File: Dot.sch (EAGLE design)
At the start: 43 parts, among them IC1 CAT24M010TS, IC2 SI1145, U1 ATMEGA328P-MU-QFN32, U2 TMP102, U3 ISL29125, U4 9DoF IMU, U5 BMP18

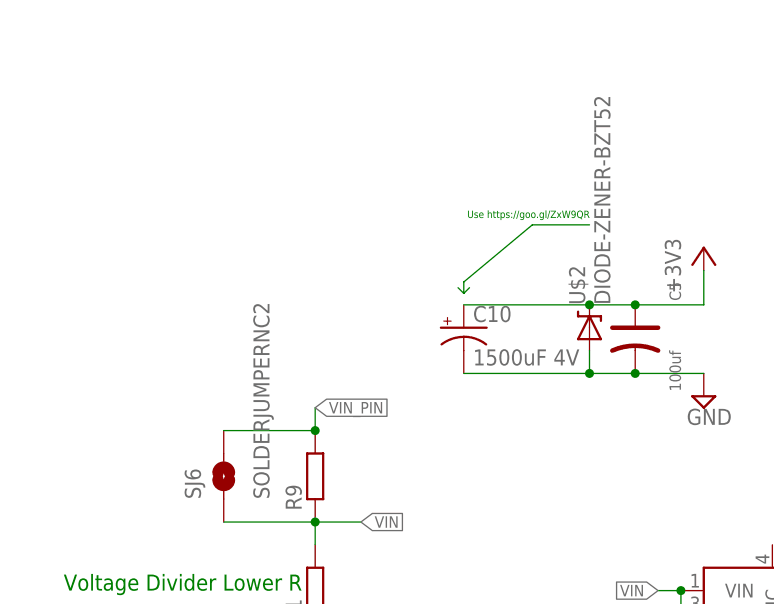
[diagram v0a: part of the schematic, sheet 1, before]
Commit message: Update description : Use a Schottky instead of R9 for solar cell
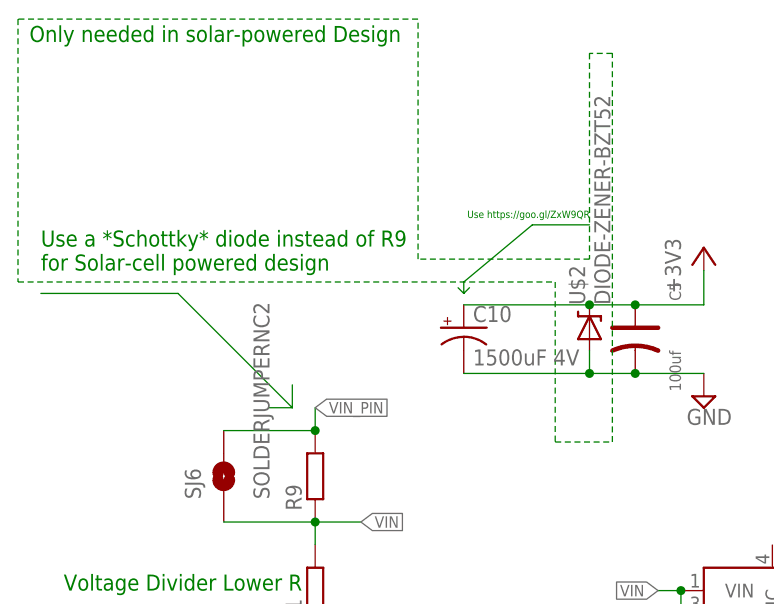
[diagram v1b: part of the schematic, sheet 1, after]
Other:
- note added: "Only needed in solar-powered Design"
- note added: "Use a *Schottky* diode instead of R9 for Solar-cell powered design"
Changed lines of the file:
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@@
 <setting verticaltext="up"/>
 </settings>
-<grid distance="1.27" unitdist="mm" unit="mm" style="lines" multiple="1" display="no" altdistance="0.01" altunitdist="inch" altunit="inch"/>
+<grid distance="0.1" unitdist="inch" unit="inch" style="lines" multiple="1" display="no" altdistance="0.01" altunitdist="inch" altunit="inch"/>
 <layers>
 <layer number="1" name="Top" color="4" fill="1" visible="no" active="no"/>
@@
 <text x="-60.96" y="134.62" size="1.778" layer="91">Voltage Divider Lower R</text>
 <text x="-16.129" y="176.022" size="0.8128" layer="91">Use https://goo.gl/ZxW9QR</text>
+<text x="-63.5" y="170.18" size="1.778" layer="91">Use a *Schottky* diode instead of R9
+for Solar-cell powered design</text>
+<text x="-64.77" y="195.58" size="1.778" layer="91">Only needed in solar-powered Design</text>
 </plain>
 <instances>
@@
 </segment>
 </net>
+<net name="N$9" class="0">
+<segment>
+<wire x1="-63.5" y1="167.64" x2="-48.26" y2="167.64" width="0.1524" layer="91"/>
+<wire x1="-48.26" y1="167.64" x2="-35.56" y2="154.94" width="0.1524" layer="91"/>
+<wire x1="-35.56" y1="154.94" x2="-35.56" y2="157.48" width="0.1524" layer="91"/>
+<wire x1="-35.56" y1="154.94" x2="-38.1" y2="154.94" width="0.1524" layer="91"/>
+</segment>
+</net>
+<net name="N$12" class="0">
+<segment>
+<wire x1="-66.04" y1="168.91" x2="-6.35" y2="168.91" width="0.1524" layer="91" style="shortdash"/>
+<wire x1="-6.35" y1="168.91" x2="-6.35" y2="151.13" width="0.1524" layer="91" style="shortdash"/>
+<wire x1="-6.35" y1="151.13" x2="0" y2="151.13" width="0.1524" layer="91" style="shortdash"/>
+<wire x1="0" y1="151.13" x2="0" y2="194.31" width="0.1524" layer="91" style="shortdash"/>
+<wire x1="0" y1="194.31" x2="-2.54" y2="194.31" width="0.1524" layer="91" style="shortdash"/>
+<wire x1="-2.54" y1="194.31" x2="-2.54" y2="171.45" width="0.1524" layer="91" style="shortdash"/>
+<wire x1="-2.54" y1="171.45" x2="-21.59" y2="171.45" width="0.1524" layer="91" style="shortdash"/>
+<wire x1="-21.59" y1="171.45" x2="-21.59" y2="198.12" width="0.1524" layer="91" style="shortdash"/>
+<wire x1="-21.59" y1="198.12" x2="-66.04" y2="198.12" width="0.1524" layer="91" style="shortdash"/>
+<wire x1="-66.04" y1="198.12" x2="-66.04" y2="168.91" width="0.1524" layer="91" style="shortdash"/>
+</segment>
+</net>

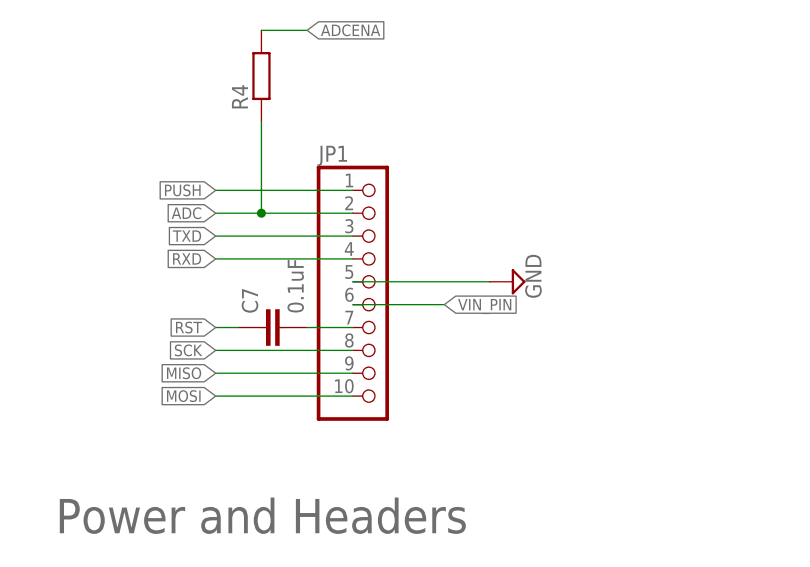
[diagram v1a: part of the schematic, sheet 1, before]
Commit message: Add jumper for C7 Reset
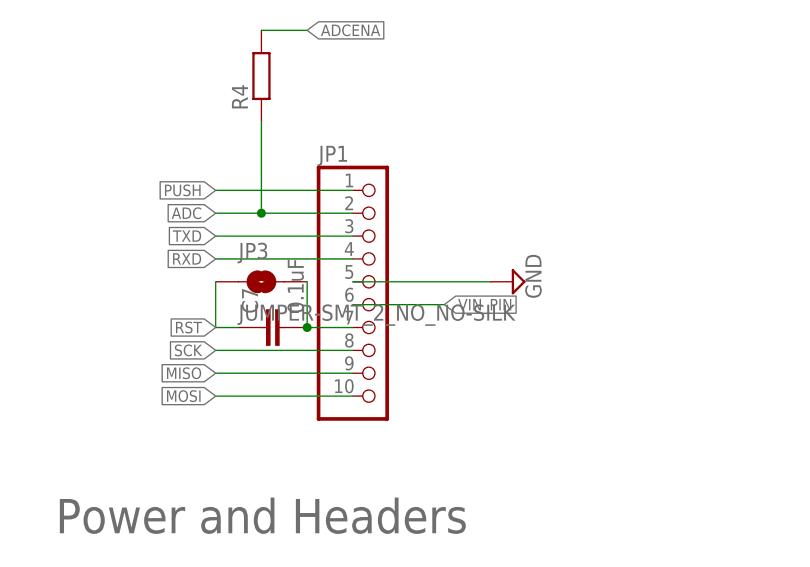
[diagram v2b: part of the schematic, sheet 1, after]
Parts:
- added JP3: JUMPER-SMT_2_NO_NO-SILK, SparkFun-Jumpers:JUMPER-SMT_2_NO_NO-SILK
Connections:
- net N$5: now also JP3.2
- net RST: now also JP3.1
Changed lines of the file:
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@@
 <part name="C10" library="adafruit" deviceset="CPOL-US" device="CT7343" value="1500uF 4V"/>
 <part name="U$2" library="SparkFun" deviceset="DIODE-ZENER" device="-BZT52"/>
+<part name="JP3" library="SparkFun-Jumpers" deviceset="JUMPER-SMT_2_NO" device="_NO-SILK"/>
 </parts>
 <sheets>
@@
 <instance part="C10" gate="G$1" x="-16.51" y="163.83"/>
 <instance part="U$2" gate="G$1" x="-2.54" y="163.83" rot="R90"/>
+<instance part="JP3" gate="G$1" x="66.04" y="134.62"/>
 </instances>
 <busses>
@@
 <wire x1="63.5" y1="129.54" x2="60.96" y2="129.54" width="0.1524" layer="91"/>
 <label x="60.96" y="129.54" size="1.27" layer="95" rot="R180" xref="yes"/>
+<wire x1="60.96" y1="134.62" x2="60.96" y2="129.54" width="0.1524" layer="91"/>
+<pinref part="JP3" gate="G$1" pin="1"/>
 </segment>
 </net>
@@
 <pinref part="C7" gate="G$1" pin="2"/>
 <wire x1="76.2" y1="129.54" x2="71.12" y2="129.54" width="0.1524" layer="91"/>
-</segment>
-</net>
+<wire x1="71.12" y1="134.62" x2="71.12" y2="129.54" width="0.1524" layer="91"/>
+<junction x="71.12" y="129.54"/>
+<pinref part="JP3" gate="G$1" pin="2"/>
+</segment>
+</net>

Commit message: Added AT25SF081, fixed labels
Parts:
- removed C6: 1uF, resistor:C-EUC0603
- removed SJ6: SOLDERJUMPERNC2, SparkFun:SOLDERJUMPERNC2
- added JP4: JUMPER-SMT_2_NO_NO-SILK, SparkFun-Jumpers:JUMPER-SMT_2_NO_NO-SILK
- C7: value 0.1uF -> 1uF
- U$3: value AT45DB641E -> AT25SF081; device AT45DB641E:AT45DB641E -> AT25SF081:AT25SF081
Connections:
- net +3V3: now also U$3.NHOLD, U$3.WP; no longer C6.1, U$3.NRST
- net GND: no longer C6.2, U$3.PAD
- net VIN: now also JP4.2; no longer SJ6.1
- net VIN_PIN: now also JP4.1; no longer SJ6.2
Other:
- note added: "Use AT25SF081-MAHF-T"
- note removed: "use AT45DB641E-MHN-Y for starndard page size (1056b/page) or AT45DB641E-MHN2B-T for binary page size (1024b/page)"
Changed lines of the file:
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@@
 <part name="SUPPLY20" library="supply2" deviceset="GND" device=""/>
 <part name="U3" library="SparkFun-Sensors" deviceset="ISL29125" device=""/>
-<part name="C6" library="resistor" deviceset="C-EU" device="C0603" value="1uF"/>
 <part name="SUPPLY21" library="supply2" deviceset="GND" device=""/>
 <part name="U4" library="SparkFun-Sensors" deviceset="MPU-9250" device="" value="9DoF IMU"/>
@@
 <part name="+3V14" library="supply1" deviceset="+3V3" device=""/>
 <part name="U5" library="Seeed-OPL-sensor" deviceset="PRESSURE-BMP180(LGA7)" device="" value="BMP18"/>
-<part name="U$3" library="AT45DB641E" deviceset="AT45DB641E" device=""/>
 <part name="+3V15" library="supply1" deviceset="+3V3" device=""/>
 <part name="SUPPLY7" library="supply2" deviceset="GND" device=""/>
@@
 <part name="R9" library="resistor" deviceset="R-EU_" device="R0603"/>
 <part name="SJ3" library="SparkFun" deviceset="SOLDERJUMPER" device="NC2"/>
-<part name="C7" library="resistor" deviceset="C-EU" device="C0603" value="0.1uF"/>
-<part name="SJ6" library="SparkFun" deviceset="SOLDERJUMPER" device="NC2"/>
+<part name="C7" library="resistor" deviceset="C-EU" device="C0603" value="1uF"/>
 <part name="Y1" library="SparkFun-Clocks" deviceset="RESONATOR" device="SMD-3.2X1.3"/>
 <part name="SUPPLY30" library="supply2" deviceset="GND" device=""/>
@@
 <part name="U$2" library="SparkFun" deviceset="DIODE-ZENER" device="-BZT52"/>
 <part name="JP3" library="SparkFun-Jumpers" deviceset="JUMPER-SMT_2_NO" device="_NO-SILK"/>
+<part name="JP4" library="SparkFun-Jumpers" deviceset="JUMPER-SMT_2_NO" device="_NO-SILK"/>
+<part name="U$3" library="AT25SF081" deviceset="AT25SF081" device=""/>
 </parts>
 <sheets>
@@
 Humidity</text>
 <text x="175.26" y="0" size="1.016" layer="91" align="center">TMP102 or TMP112 (high acc +/-0.5°)</text>
-<text x="43.18" y="88.9" size="1.778" layer="91">use AT45DB641E-MHN-Y for starndard page size (1056b/page)
-or AT45DB641E-MHN2B-T for binary page size (1024b/page)</text>
 <text x="-24.13" y="50.8" size="1.27" layer="91">Blue</text>
 <text x="-7.62" y="50.8" size="1.27" layer="91" rot="R90">Green</text>
@@
 for Solar-cell powered design</text>
 <text x="-64.77" y="195.58" size="1.778" layer="91">Only needed in solar-powered Design</text>
+<text x="73.66" y="86.36" size="1.778" layer="91">Use AT25SF081-MAHF-T</text>
 </plain>
 <instances>
@@
 <instance part="SUPPLY20" gate="GND" x="264.16" y="-38.1" rot="MR0"/>
 <instance part="U3" gate="G$1" x="358.14" y="-27.94"/>
-<instance part="C6" gate="G$1" x="337.82" y="-27.94"/>
 <instance part="SUPPLY21" gate="GND" x="337.82" y="-35.56" rot="MR0"/>
 <instance part="U4" gate="G$1" x="78.74" y="-27.94"/>
@@
 <instance part="+3V14" gate="G$1" x="-10.16" y="81.28"/>
 <instance part="U5" gate="G$1" x="170.18" y="-50.8"/>
-<instance part="U$3" gate="G$1" x="60.96" y="68.58"/>
-<instance part="+3V15" gate="G$1" x="96.52" y="83.82"/>
-<instance part="SUPPLY7" gate="GND" x="91.44" y="73.66" rot="R90"/>
-<instance part="+3V17" gate="G$1" x="48.26" y="78.74"/>
-<instance part="SUPPLY8" gate="GND" x="73.66" y="81.28" rot="R90"/>
+<instance part="+3V15" gate="G$1" x="111.76" y="83.82"/>
+<instance part="SUPPLY7" gate="GND" x="66.04" y="68.58" rot="R270"/>
+<instance part="+3V17" gate="G$1" x="55.88" y="71.12" rot="R90"/>
+<instance part="SUPPLY8" gate="GND" x="45.72" y="93.98" rot="R90"/>
 <instance part="+3V18" gate="G$1" x="154.94" y="-43.18"/>
 <instance part="SUPPLY22" gate="GND" x="166.37" y="-60.96" rot="MR0"/>
@@
 <instance part="SJ3" gate="1" x="17.78" y="114.3"/>
 <instance part="C7" gate="G$1" x="66.04" y="129.54" rot="R90"/>
-<instance part="SJ6" gate="1" x="-43.18" y="147.32" rot="R90"/>
 <instance part="Y1" gate="G$1" x="200.66" y="66.04" rot="R90"/>
 <instance part="SUPPLY30" gate="GND" x="208.28" y="63.5"/>
@@
 <instance part="U$2" gate="G$1" x="-2.54" y="163.83" rot="R90"/>
 <instance part="JP3" gate="G$1" x="66.04" y="134.62"/>
+<instance part="JP4" gate="G$1" x="-43.18" y="147.32" rot="MR270"/>
+<instance part="U$3" gate="G$1" x="71.12" y="68.58"/>
 </instances>
 <busses>
@@
 </segment>
 <segment>
-<pinref part="C6" gate="G$1" pin="2"/>
 <pinref part="U3" gate="G$1" pin="GND"/>
 <wire x1="337.82" y1="-33.02" x2="347.98" y2="-33.02" width="0.1524" layer="91"/>
 <wire x1="347.98" y1="-33.02" x2="347.98" y2="-30.48" width="0.1524" layer="91"/>
-<junction x="337.82" y="-33.02"/>
 <pinref part="SUPPLY21" gate="GND" pin="GND"/>
 </segment>
@@
 </segment>
 <segment>
+<pinref part="SUPPLY7" gate="GND" pin="GND"/>
+<wire x1="71.12" y1="68.58" x2="68.58" y2="68.58" width="0.1524" layer="91"/>
 <pinref part="U$3" gate="G$1" pin="GND"/>
-<pinref part="SUPPLY7" gate="GND" pin="GND"/>
-<wire x1="81.28" y1="73.66" x2="88.9" y2="73.66" width="0.1524" layer="91"/>
-</segment>
-<segment>
-<pinref part="U$3" gate="G$1" pin="PAD"/>
-<pinref part="SUPPLY8" gate="GND" pin="GND"/>
 </segment>
 <segment>
@@
 <pinref part="+3V9" gate="G$1" pin="+3V3"/>
 <pinref part="C1" gate="G$1" pin="1"/>
-<pinref part="C6" gate="G$1" pin="1"/>
 <pinref part="U3" gate="G$1" pin="VDD"/>
-<wire x1="337.82" y1="-25.4" x2="347.98" y2="-25.4" width="0.1524" layer="91"/>
-<wire x1="327.66" y1="-25.4" x2="337.82" y2="-25.4" width="0.1524" layer="91"/>
+<wire x1="327.66" y1="-25.4" x2="347.98" y2="-25.4" width="0.1524" layer="91"/>
 <junction x="327.66" y="-25.4"/>
-<junction x="337.82" y="-25.4"/>
 </segment>
 <segment>
@@
 </segment>
 <segment>
+<pinref part="+3V15" gate="G$1" pin="+3V3"/>
+<wire x1="101.6" y1="76.2" x2="111.76" y2="76.2" width="0.1524" layer="91"/>
+<wire x1="111.76" y1="76.2" x2="111.76" y2="81.28" width="0.1524" layer="91"/>
 <pinref part="U$3" gate="G$1" pin="VCC"/>
-<pinref part="+3V15" gate="G$1" pin="+3V3"/>
-<wire x1="81.28" y1="71.12" x2="96.52" y2="71.12" width="0.1524" layer="91"/>
-<wire x1="96.52" y1="71.12" x2="96.52" y2="81.28" width="0.1524" layer="91"/>
-</segment>
-<segment>
-<pinref part="U$3" gate="G$1" pin="NRST"/>
+<pinref part="U$3" gate="G$1" pin="NHOLD"/>
+<wire x1="101.6" y1="73.66" x2="111.76" y2="73.66" width="0.1524" layer="91"/>
+<wire x1="111.76" y1="73.66" x2="111.76" y2="76.2" width="0.1524" layer="91"/>
+<junction x="111.76" y="76.2"/>
+</segment>
+<segment>
 <pinref part="+3V17" gate="G$1" pin="+3V3"/>
-<wire x1="60.96" y1="71.12" x2="48.26" y2="71.12" width="0.1524" layer="91"/>
-<wire x1="48.26" y1="71.12" x2="48.26" y2="76.2" width="0.1524" layer="91"/>
+<wire x1="71.12" y1="71.12" x2="58.42" y2="71.12" width="0.1524" layer="91"/>
+<pinref part="U$3" gate="G$1" pin="WP"/>
 </segment>
 <segment>
@@
 </segment>
 <segment>
+<wire x1="101.6" y1="68.58" x2="111.76" y2="68.58" width="0.1524" layer="91"/>
+<label x="111.76" y="68.58" size="1.27" layer="95" xref="yes"/>
 <pinref part="U$3" gate="G$1" pin="SI"/>
-<wire x1="60.96" y1="76.2" x2="58.42" y2="76.2" width="0.1524" layer="91"/>
-<label x="58.42" y="76.2" size="1.27" layer="95" rot="R180" xref="yes"/>
 </segment>
 </net>
@@
 </segment>
 <segment>
+<wire x1="71.12" y1="73.66" x2="63.5" y2="73.66" width="0.1524" layer="91"/>
+<label x="63.5" y="73.66" size="1.27" layer="95" rot="R180" xref="yes"/>
 <pinref part="U$3" gate="G$1" pin="SO"/>
-<wire x1="81.28" y1="76.2" x2="83.82" y2="76.2" width="0.1524" layer="91"/>
-<label x="83.82" y="76.2" size="1.27" layer="95" xref="yes"/>
 </segment>
 </net>
@@
 </segment>
 <segment>
+<wire x1="101.6" y1="71.12" x2="111.76" y2="71.12" width="0.1524" layer="91"/>
+<label x="111.76" y="71.12" size="1.27" layer="95" xref="yes"/>
 <pinref part="U$3" gate="G$1" pin="SCK"/>
-<wire x1="60.96" y1="73.66" x2="58.42" y2="73.66" width="0.1524" layer="91"/>
-<label x="58.42" y="73.66" size="1.27" layer="95" rot="R180" xref="yes"/>
 </segment>
 </net>
@@
 <net name="FLASH_CS" class="0">
 <segment>
+<wire x1="71.12" y1="76.2" x2="63.5" y2="76.2" width="0.1524" layer="91"/>
+<label x="63.5" y="76.2" size="1.27" layer="95" rot="R180" xref="yes"/>
 <pinref part="U$3" gate="G$1" pin="CS"/>
-<wire x1="60.96" y1="68.58" x2="58.42" y2="68.58" width="0.1524" layer="91"/>
-<label x="58.42" y="68.58" size="1.27" layer="95" rot="R180" xref="yes"/>
 </segment>
 <segment>
@@
 <junction x="-33.02" y="142.24"/>
 <label x="-27.94" y="142.24" size="1.27" layer="95" xref="yes"/>
-<pinref part="SJ6" gate="1" pin="1"/>
 <wire x1="-43.18" y1="142.24" x2="-33.02" y2="142.24" width="0.1524" layer="91"/>
+<pinref part="JP4" gate="G$1" pin="2"/>
 </segment>
 </net>
@@
 <wire x1="-33.02" y1="152.4" x2="-33.02" y2="154.94" width="0.1524" layer="91"/>
 <label x="-33.02" y="154.94" size="1.27" layer="95" xref="yes"/>
-<pinref part="SJ6" gate="1" pin="2"/>
 <wire x1="-43.18" y1="152.4" x2="-33.02" y2="152.4" width="0.1524" layer="91"/>
 <junction x="-33.02" y="152.4"/>
-</segment>
-<segment>
+<pinref part="JP4" gate="G$1" pin="1"/>
+</segment>
+<segment>
